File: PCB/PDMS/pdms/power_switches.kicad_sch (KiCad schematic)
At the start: 8 parts

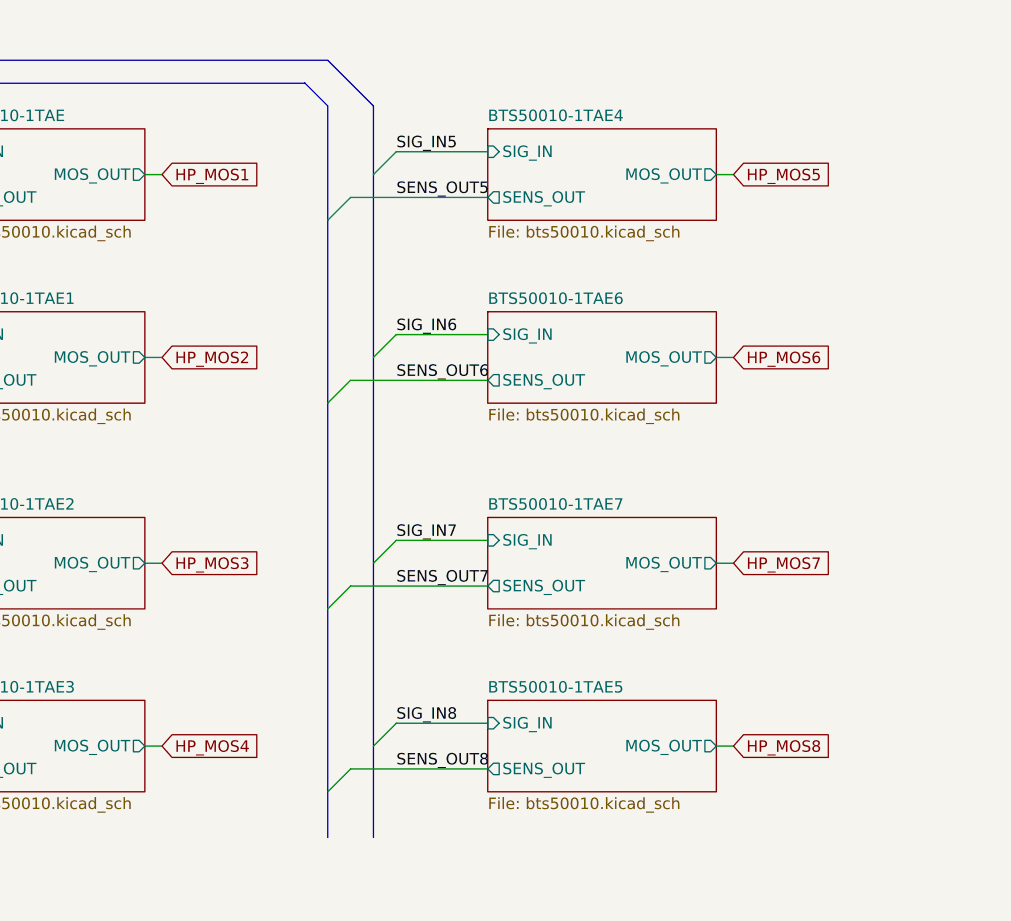
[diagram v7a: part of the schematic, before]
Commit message: Layout of high current traces to connector changed
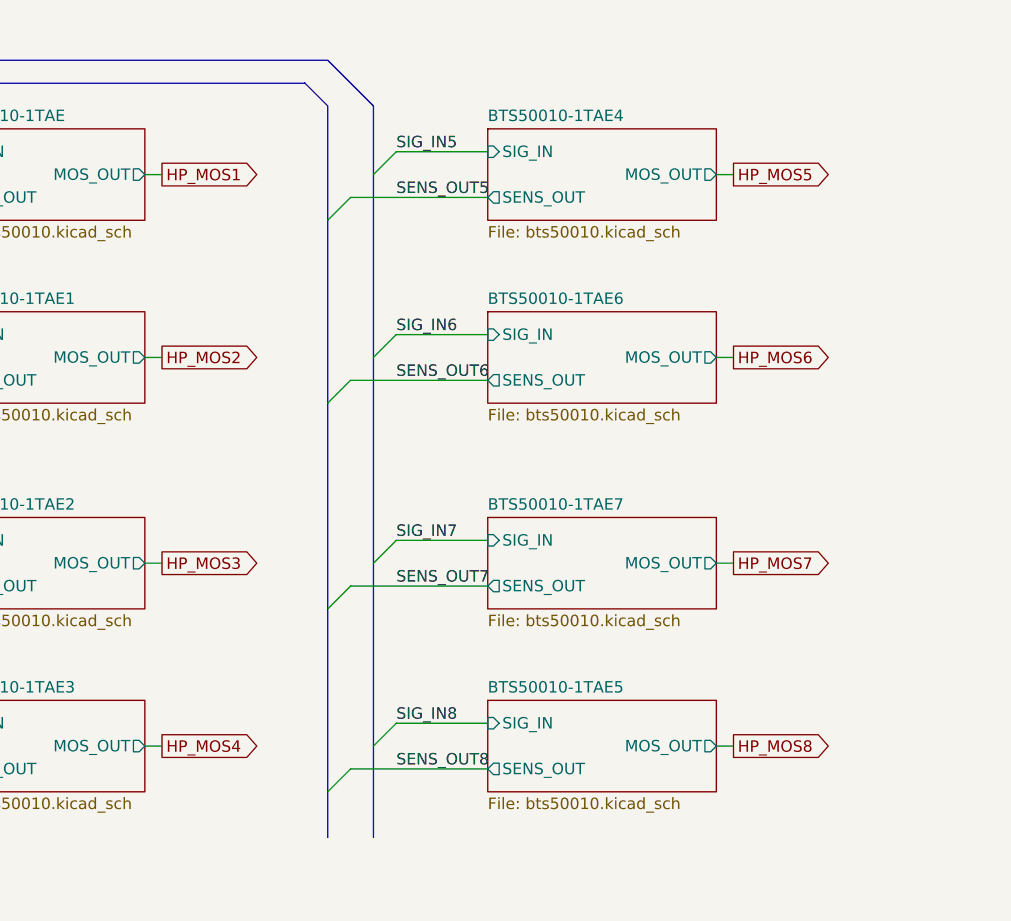
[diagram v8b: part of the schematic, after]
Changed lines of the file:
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@@
     (effects (font (size 1.27 1.27)) (justify left bottom))
+  )
+  (global_label "HP_MOS1" (shape output) (at 90.805 68.58 0) (fields_autoplaced)
+    (effects (font (size 1.27 1.27)) (justify left))
+    (property "Intersheet References" "${INTERSHEET_REFS}" (id 0) (at 101.9871 68.5006 0)
+      (effects (font (size 1.27 1.27)) (justify left) hide)
+    )
   )
   (global_label "LP_CSN1" (shape input) (at 220.98 78.74 270) (fields_autoplaced)
@@
     )
   )
-  (global_label "HP_MOS8" (shape input) (at 154.305 132.08 0) (fields_autoplaced)
-    (effects (font (size 1.27 1.27)) (justify left))
-    (property "Intersheet References" "${INTERSHEET_REFS}" (id 0) (at 165.4871 132.0006 0)
-      (effects (font (size 1.27 1.27)) (justify left) hide)
-    )
-  )
-  (global_label "HP_MOS1" (shape input) (at 90.805 68.58 0) (fields_autoplaced)
-    (effects (font (size 1.27 1.27)) (justify left))
-    (property "Intersheet References" "${INTERSHEET_REFS}" (id 0) (at 101.9871 68.5006 0)
-      (effects (font (size 1.27 1.27)) (justify left) hide)
-    )
-  )
   (global_label "LP_MOS1" (shape input) (at 237.49 53.34 0) (fields_autoplaced)
     (effects (font (size 1.27 1.27)) (justify left))
@@
     )
   )
-  (global_label "HP_MOS4" (shape input) (at 90.805 132.08 0) (fields_autoplaced)
+  (global_label "HP_MOS2" (shape output) (at 90.805 88.9 0) (fields_autoplaced)
     (effects (font (size 1.27 1.27)) (justify left))
-    (property "Intersheet References" "${INTERSHEET_REFS}" (id 0) (at 101.9871 132.0006 0)
+    (property "Intersheet References" "${INTERSHEET_REFS}" (id 0) (at 101.9871 88.8206 0)
       (effects (font (size 1.27 1.27)) (justify left) hide)
     )
@@
     )
   )
-  (global_label "HP_MOS7" (shape input) (at 154.305 111.76 0) (fields_autoplaced)
+  (global_label "HP_MOS5" (shape output) (at 154.305 68.58 0) (fields_autoplaced)
     (effects (font (size 1.27 1.27)) (justify left))
-    (property "Intersheet References" "${INTERSHEET_REFS}" (id 0) (at 165.4871 111.6806 0)
-      (effects (font (size 1.27 1.27)) (justify left) hide)
-    )
-  )
-  (global_label "HP_MOS3" (shape input) (at 90.805 111.76 0) (fields_autoplaced)
-    (effects (font (size 1.27 1.27)) (justify left))
-    (property "Intersheet References" "${INTERSHEET_REFS}" (id 0) (at 101.9871 111.6806 0)
+    (property "Intersheet References" "${INTERSHEET_REFS}" (id 0) (at 165.4871 68.5006 0)
       (effects (font (size 1.27 1.27)) (justify left) hide)
     )
@@
     )
   )
+  (global_label "HP_MOS8" (shape output) (at 154.305 132.08 0) (fields_autoplaced)
+    (effects (font (size 1.27 1.27)) (justify left))
+    (property "Intersheet References" "${INTERSHEET_REFS}" (id 0) (at 165.4871 132.0006 0)
+      (effects (font (size 1.27 1.27)) (justify left) hide)
+    )
+  )
   (global_label "SENS_OUT_LP1" (shape output) (at 203.2 71.12 180) (fields_autoplaced)
     (effects (font (size 1.27 1.27)) (justify right))
     (property "Intersheet References" "${INTERSHEET_REFS}" (id 0) (at 186.8169 71.1994 0)
       (effects (font (size 1.27 1.27)) (justify right) hide)
+    )
+  )
+  (global_label "HP_MOS4" (shape output) (at 90.805 132.08 0) (fields_autoplaced)
+    (effects (font (size 1.27 1.27)) (justify left))
+    (property "Intersheet References" "${INTERSHEET_REFS}" (id 0) (at 101.9871 132.0006 0)
+      (effects (font (size 1.27 1.27)) (justify left) hide)
     )
   )
@@
     )
   )
-  (global_label "HP_MOS5" (shape input) (at 154.305 68.58 0) (fields_autoplaced)
-    (effects (font (size 1.27 1.27)) (justify left))
-    (property "Intersheet References" "${INTERSHEET_REFS}" (id 0) (at 165.4871 68.5006 0)
-      (effects (font (size 1.27 1.27)) (justify left) hide)
-    )
-  )
   (global_label "SENS_OUT[1..8]" (shape input) (at 45.72 50.8 180) (fields_autoplaced)
     (effects (font (size 1.27 1.27)) (justify right))
@@
     )
   )
-  (global_label "HP_MOS6" (shape input) (at 154.305 88.9 0) (fields_autoplaced)
+  (global_label "HP_MOS6" (shape output) (at 154.305 88.9 0) (fields_autoplaced)
     (effects (font (size 1.27 1.27)) (justify left))
     (property "Intersheet References" "${INTERSHEET_REFS}" (id 0) (at 165.4871 88.8206 0)
@@
     )
   )
-  (global_label "HP_MOS2" (shape input) (at 90.805 88.9 0) (fields_autoplaced)
+  (global_label "HP_MOS3" (shape output) (at 90.805 111.76 0) (fields_autoplaced)
     (effects (font (size 1.27 1.27)) (justify left))
-    (property "Intersheet References" "${INTERSHEET_REFS}" (id 0) (at 101.9871 88.8206 0)
+    (property "Intersheet References" "${INTERSHEET_REFS}" (id 0) (at 101.9871 111.6806 0)
       (effects (font (size 1.27 1.27)) (justify left) hide)
     )
+  )
+  (global_label "HP_MOS7" (shape output) (at 154.305 111.76 0) (fields_autoplaced)
+    (effects (font (size 1.27 1.27)) (justify left))
+    (property "Intersheet References" "${INTERSHEET_REFS}" (id 0) (at 165.4871 111.6806 0)
+      (effects (font (size 1.27 1.27)) (justify left) hide)
+    )
